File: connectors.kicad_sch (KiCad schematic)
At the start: 65 parts, among them J1 Molex_Nano-Fit_1x2_SMD_105430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, J2 Conn_FAKRA_59S2AQ-40MT5-Z_1, J3 Conn_FAKRA_59S2AQ-40MT5-Z_1, J4 Conn_FAKRA_59S2AQ-40MT5-Z_1, J5 Conn_FAKRA_59S2AQ-40MT5-Z_1, J6 Conn_FFC_WE_68715014522, Q6 DMG1012T-7, U1 SN74LV1T125DBVR, U2 SN74LV1T125DBVR, U8 NTS0102_TSSOP

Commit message: [#74135] Fix DNP malformations
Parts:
- R61, R63, R68, R69, R8: DNP DNP -> (none)
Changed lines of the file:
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@@
 			)
 		)
-		(property "DNP" "DNP"
-			(at 116.84 143.51 0)
-			(effects
-				(font
-					(size 1.27 1.27)
-				)
-				(hide yes)
-			)
-		)
 		(pin "1"
 		)
@@
 			)
 		)
-		(property "DNP" "DNP"
-			(at 116.84 139.7 0)
-			(effects
-				(font
-					(size 1.27 1.27)
-				)
-				(hide yes)
-			)
-		)
 		(pin "1"
 		)
@@
 			)
 		)
-		(property "DNP" "DNP"
-			(at 190.5 128.27 0)
-			(effects
-				(font
-					(size 1.27 1.27)
-				)
-				(hide yes)
-			)
-		)
 		(pin "1"
 		)
@@
 			)
 		)
-		(property "DNP" "DNP"
-			(at 289.56 160.02 0)
-			(effects
-				(font
-					(size 1.27 1.27)
-				)
-				(hide yes)
-			)
-		)
 		(pin "1"
 		)
@@
 				(hide yes)
 			)
-		)
-		(property "DNP" "DNP"
-			(at 184.15 128.27 0)
-			(effects
-				(font
-					(size 1.27 1.27)
-				)
-				(hide yes)
-			)

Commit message: [#74135] Clean noInBom fields
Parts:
- Q6: now in the parts list
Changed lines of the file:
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@@
 	(label "FFC_3V3"
 		(at 259.08 199.39 270)
-		(fields_autoplaced yes)
 		(effects
 			(font
@@
 	(label "VSYNC_CAM0"
 		(at 106.68 72.39 0)
-		(fields_autoplaced yes)
 		(effects
 			(font
@@
 	(label "CSI0.CLK_P"
 		(at 331.47 104.14 0)
-		(fields_autoplaced yes)
 		(effects
 			(font
@@
 	(label "MFP1"
 		(at 156.21 76.2 180)
-		(fields_autoplaced yes)
 		(effects
 			(font
@@
 	(label "MFP1"
 		(at 53.34 190.5 180)
-		(fields_autoplaced yes)
 		(effects
 			(font
@@
 	(label "MFP0"
 		(at 156.21 72.39 180)
-		(fields_autoplaced yes)
 		(effects
 			(font
@@
 	(label "CSI0.D1_N"
 		(at 331.47 88.9 0)
-		(fields_autoplaced yes)
 		(effects
 			(font
@@
 	(label "CSI1.CLK_N"
 		(at 331.47 147.32 0)
-		(fields_autoplaced yes)
 		(effects
 			(font
@@
 	(label "MFP3"
 		(at 53.34 195.58 180)
-		(fields_autoplaced yes)
 		(effects
 			(font
@@
 	(label "SCL_CAM0"
 		(at 337.82 177.8 0)
-		(fields_autoplaced yes)
 		(effects
 			(font
@@
 	(label "MFP5"
 		(at 53.34 200.66 180)
-		(fields_autoplaced yes)
 		(effects
 			(font
@@
 	(label "VSYNC_CAM1"
 		(at 261.62 162.56 0)
-		(fields_autoplaced yes)
 		(effects
 			(font
@@
 	(label "CSI0.CLK_N"
 		(at 331.47 101.6 0)
-		(fields_autoplaced yes)
 		(effects
 			(font
@@
 	(label "SCL_CAM"
 		(at 201.93 134.62 180)
-		(fields_autoplaced yes)
 		(effects
 			(font
@@
 	(label "FFC_3V3"
 		(at 190.5 113.03 270)
-		(fields_autoplaced yes)
 		(effects
 			(font
@@
 	(label "MFP7"
 		(at 53.34 203.2 180)
-		(fields_autoplaced yes)
 		(effects
 			(font
@@
 	(label "VSYNC_CAM0"
 		(at 261.62 157.48 0)
-		(fields_autoplaced yes)
 		(effects
 			(font
@@
 	(label "CSI1.D0_N"
 		(at 331.47 139.7 0)
-		(fields_autoplaced yes)
 		(effects
 			(font
@@
 	(label "CSI1.D3_N"
 		(at 331.47 124.46 0)
-		(fields_autoplaced yes)
 		(effects
 			(font
@@
 	(label "CSI0.D2_P"
 		(at 331.47 86.36 0)
-		(fields_autoplaced yes)
 		(effects
 			(font
@@
 	(label "SDA_CAM1"
 		(at 337.82 180.34 0)
-		(fields_autoplaced yes)
 		(effects
 			(font
@@
 	(label "SCL_CAM"
 		(at 292.1 177.8 0)
-		(fields_autoplaced yes)
 		(effects
 			(font
@@
 	(label "CSI0.D2_N"
 		(at 331.47 83.82 0)
-		(fields_autoplaced yes)
 		(effects
 			(font
@@
 	(label "SDA_CAM0"
 		(at 337.82 175.26 0)
-		(fields_autoplaced yes)
 		(effects
 			(font
@@
 	(label "SCL_CAM1"
 		(at 337.82 182.88 0)
-		(fields_autoplaced yes)
 		(effects
 			(font
@@
 	(label "CSI0.D0_P"
 		(at 331.47 96.52 0)
-		(fields_autoplaced yes)
 		(effects
 			(font
@@
 	(label "CSI1.CLK_P"
 		(at 331.47 149.86 0)
-		(fields_autoplaced yes)
 		(effects
 			(font
@@
 	(label "CSI0.D1_P"
 		(at 331.47 91.44 0)
-		(fields_autoplaced yes)
 		(effects
 			(font
@@
 	(label "MFP8"
 		(at 53.34 205.74 180)
-		(fields_autoplaced yes)
 		(effects
 			(font
@@
 	(label "SDA_CAM"
 		(at 201.93 132.08 180)
-		(fields_autoplaced yes)
 		(effects
 			(font
@@
 	(label "MFP7"
 		(at 101.6 139.7 0)
-		(fields_autoplaced yes)
 		(effects
 			(font
@@
 	(label "FFC_3V3"
 		(at 294.64 195.58 0)
-		(fields_autoplaced yes)
 		(effects
 			(font
@@
 	(label "CSI1.D3_P"
 		(at 331.47 127 0)
-		(fields_autoplaced yes)
 		(effects
 			(font
@@
 	(label "CSI1.D1_N"
 		(at 331.47 134.62 0)
-		(fields_autoplaced yes)
 		(effects
 			(font
@@
 	(label "CSI0.D3_P"
 		(at 331.47 81.28 0)
-		(fields_autoplaced yes)
 		(effects
 			(font
@@
 	(label "SDA_CAM"
 		(at 292.1 175.26 0)
-		(fields_autoplaced yes)
 		(effects
 			(font
@@
 	(label "CSI1.D1_P"
 		(at 331.47 137.16 0)
-		(fields_autoplaced yes)
 		(effects
 			(font
@@
 	(label "DC_UNFUSED"
 		(at 29.21 69.85 0)
-		(fields_autoplaced yes)
 		(effects
 			(font
@@
 	(label "CSI1.D2_P"
 		(at 331.47 132.08 0)
-		(fields_autoplaced yes)
 		(effects
 			(font
@@
 	(label "CSI1.D2_N"
 		(at 331.47 129.54 0)
-		(fields_autoplaced yes)
 		(effects
 			(font
@@
 	(label "MFP3"
 		(at 210.82 76.2 180)
-		(fields_autoplaced yes)
 		(effects
 			(font
@@
 	(label "MFP8"
 		(at 101.6 143.51 0)
-		(fields_autoplaced yes)
 		(effects
 			(font
@@
 	(label "MFP4"
 		(at 20.32 246.38 0)
-		(fields_autoplaced yes)
 		(effects
 			(font
@@
 	(label "CSI0.D0_N"
 		(at 331.47 93.98 0)
-		(fields_autoplaced yes)
 		(effects
 			(font
@@
 	(label "MFP0"
 		(at 53.34 187.96 180)
-		(fields_autoplaced yes)
 		(effects
 			(font
@@
 	(label "FFC_3V3"
 		(at 175.26 105.41 270)
-		(fields_autoplaced yes)
 		(effects
 			(font
@@
 	(label "MFP4"
 		(at 53.34 198.12 180)
-		(fields_autoplaced yes)
 		(effects
 			(font
@@
 	(label "CSI0.D3_N"
 		(at 331.47 78.74 0)
-		(fields_autoplaced yes)
 		(effects
 			(font
@@
 	(label "MFP2"
 		(at 210.82 72.39 180)
-		(fields_autoplaced yes)
 		(effects
 			(font
@@
 	(label "VSYNC_CAM1"
 		(at 161.29 72.39 0)
-		(fields_autoplaced yes)
 		(effects
 			(font
@@
 	(label "DC_UNFUSED"
 		(at 78.74 91.44 180)
-		(fields_autoplaced yes)
 		(effects
 			(font
@@
 	(label "CSI1.D0_P"
 		(at 331.47 142.24 0)
-		(fields_autoplaced yes)
 		(effects
 			(font
@@
 	(label "MFP2"
 		(at 53.34 193.04 180)
-		(fields_autoplaced yes)
 		(effects
 			(font
@@
 		(shape bidirectional)
 		(at 147.32 233.68 180)
-		(fields_autoplaced yes)
 		(effects
 			(font
@@
 		(shape input)
 		(at 322.58 153.67 180)
-		(fields_autoplaced yes)
 		(effects
 			(font
@@
 		(shape input)
 		(at 151.13 256.54 90)
-		(fields_autoplaced yes)
 		(effects
 			(font
@@
 		(shape input)
 		(at 151.13 209.55 90)
-		(fields_autoplaced yes)
 		(effects
 			(font
@@
 		(shape input)
 		(at 322.58 107.95 180)
-		(fields_autoplaced yes)
 		(effects
 			(font
@@
 		(shape bidirectional)
 		(at 147.32 186.69 180)
-		(fields_autoplaced yes)
 		(effects
 			(font
@@
 		(shape output)
 		(at 101.6 134.62 180)
-		(fields_autoplaced yes)
 		(effects
 			(font
@@
 		(shape bidirectional)
 		(at 101.6 132.08 180)
-		(fields_autoplaced yes)
 		(effects
 			(font
@@
 		(shape output)
 		(at 303.53 200.66 180)
-		(fields_autoplaced yes)
 		(effects
 			(font
@@
 		(shape output)
 		(at 266.7 207.01 90)
-		(fields_autoplaced yes)
 		(effects
 			(font
@@
 		(shape bidirectional)
 		(at 39.37 209.55 180)
-		(fields_autoplaced yes)
 		(effects
 			(font
@@
 		(shape bidirectional)
 		(at 147.32 210.82 180)
-		(fields_autoplaced yes)
 		(effects
 			(font
@@
 		(shape input)
 		(at 151.13 185.42 90)
-		(fields_autoplaced yes)
 		(effects
 			(font
@@
 		(shape bidirectional)
 		(at 147.32 257.81 180)
-		(fields_autoplaced yes)
 		(effects
 			(font
@@
 		(shape output)
 		(at 73.66 69.85 0)
-		(fields_autoplaced yes)
 		(effects
 			(font
@@
 		(shape input)
 		(at 151.13 232.41 90)
-		(fields_autoplaced yes)
 		(effects
 			(font
@@
 		(unit 1)
 		(exclude_from_sim no)
-		(in_bom no)
+		(in_bom yes)
 		(on_board yes)
 		(dnp no)

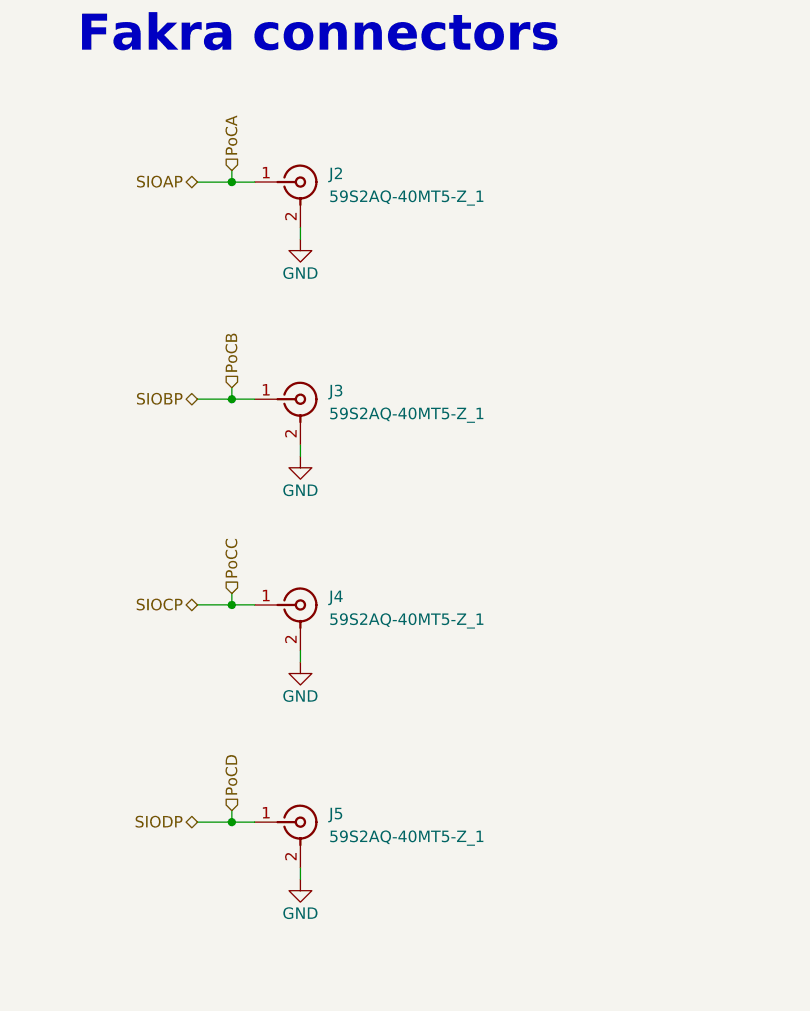
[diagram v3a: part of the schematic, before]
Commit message: [#80514] change 59S2AQ-40MT5-Z_1 connector to 7-2287906-0
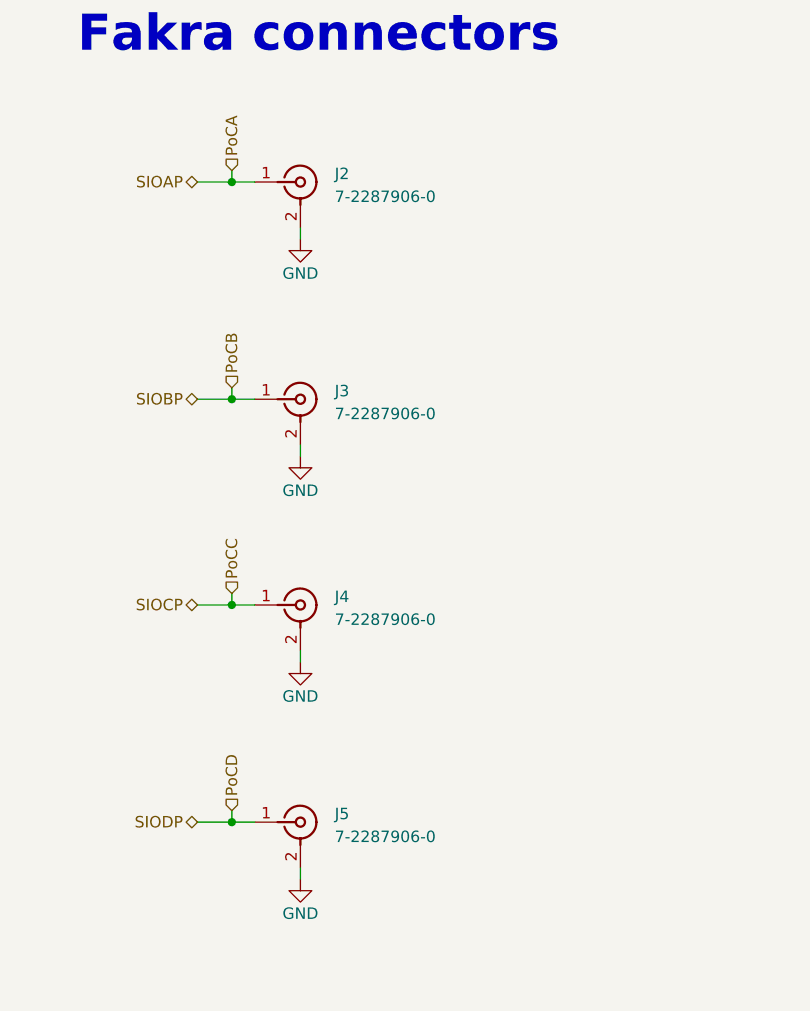
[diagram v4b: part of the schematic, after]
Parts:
- J2, J3, J4, J5: footprint antmicro-footprints:Conn_FAKRA_59S2AQ-40MT5-Z_1 -> antmicro-footprints:Conn_FAKRA_7-2287906-0; symbol antmicroCoaxialConnectorsRF:Conn_FAKRA_59S2AQ-40MT5-Z_1 -> antmicroCoaxialConnectorsRF:Conn_FAKRA_7-2287906-0; MPN 59S2AQ-40MT5-Z_1 -> 7-2287906-0; Manufacturer Rosenberger -> TE Connectivity
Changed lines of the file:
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@@
 (kicad_sch
-	(version 20231120)
+	(version 20250114)
 	(generator "eeschema")
-	(generator_version "8.0")
+	(generator_version "9.0")
 	(paper "A3")
 	(title_block
@@
 		(comment 1 "www.antmicro.com")
 	)
+	(text "Multi-function pins"
+		(exclude_from_sim no)
+		(at 21.59 177.165 0)
+		(effects
+			(font
+				(size 4 4)
+				(thickness 0.8)
+				(bold yes)
+			)
+			(justify left bottom)
+		)
+	)
+	(text "CSI connector"
+		(exclude_from_sim no)
+		(at 304.165 63.5 0)
+		(effects
+			(font
+				(size 4 4)
+				(thickness 0.8)
+				(bold yes)
+			)
+			(justify left bottom)
+		)
+	)
+	(text "Fakra connectors"
+		(exclude_from_sim no)
+		(at 133.985 172.72 0)
+		(effects
+			(font
+				(size 4 4)
+				(thickness 0.8)
+				(bold yes)
+			)
+			(justify left bottom)
+		)
+	)
+	(text "Buffer gates"
+		(exclude_from_sim no)
+		(at 143.51 40.64 0)
+		(effects
+			(font
+				(size 4 4)
+				(thickness 0.8)
+				(bold yes)
+			)
+			(justify left bottom)
+		)
+	)
+	(text "Power connector"
+		(exclude_from_sim no)
+		(at 26.035 54.61 0)
+		(effects
+			(font
+				(size 4 4)
+				(thickness 0.8)
+				(bold yes)
+			)
+			(justify left bottom)
+		)
+	)
+	(text "Level shifter"
+		(exclude_from_sim no)
+		(at 137.795 101.6 0)
+		(effects
+			(font
+				(size 4 4)
+				(thickness 0.8)
+				(bold yes)
+			)
+			(justify left bottom)
+		)
+	)
 	(junction
 		(at 289.56 157.48)
@@
 		)
 	)
-	(text "Multi-function pins"
-		(exclude_from_sim no)
-		(at 21.59 177.165 0)
-		(effects
-			(font
-				(size 4 4)
-				(thickness 0.8)
-				(bold yes)
-			)
-			(justify left bottom)
-		)
-	)
-	(text "CSI connector"
-		(exclude_from_sim no)
-		(at 304.165 63.5 0)
-		(effects
-			(font
-				(size 4 4)
-				(thickness 0.8)
-				(bold yes)
-			)
-			(justify left bottom)
-		)
-	)
-	(text "Fakra connectors"
-		(exclude_from_sim no)
-		(at 133.985 172.72 0)
-		(effects
-			(font
-				(size 4 4)
-				(thickness 0.8)
-				(bold yes)
-			)
-			(justify left bottom)
-		)
-	)
-	(text "Buffer gates"
-		(exclude_from_sim no)
-		(at 143.51 40.64 0)
-		(effects
-			(font
-				(size 4 4)
-				(thickness 0.8)
-				(bold yes)
-			)
-			(justify left bottom)
-		)
-	)
-	(text "Power connector"
-		(exclude_from_sim no)
-		(at 26.035 54.61 0)
-		(effects
-			(font
-				(size 4 4)
-				(thickness 0.8)
-				(bold yes)
-			)
-			(justify left bottom)
-		)
-	)
-	(text "Level shifter"
-		(exclude_from_sim no)
-		(at 137.795 101.6 0)
-		(effects
-			(font
-				(size 4 4)
-				(thickness 0.8)
-				(bold yes)
-			)
-			(justify left bottom)
-		)
-	)
 	(label "FFC_3V3"
 		(at 259.08 199.39 270)
@@
 	)
 	(symbol
-		(lib_id "antmicroCoaxialConnectorsRF:Conn_FAKRA_59S2AQ-40MT5-Z_1")
+		(lib_id "antmicroCoaxialConnectorsRF:Conn_FAKRA_7-2287906-0")
 		(at 153.67 210.82 0)
 		(unit 1)
@@
 		(fields_autoplaced yes)
 		(property "Reference" "J3"
-			(at 161.925 209.9066 0)
+			(at 162.56 209.9067 0)
 			(effects
 				(font
@@
 			)
 		)
-		(property "Footprint" "antmicro-footprints:Conn_FAKRA_59S2AQ-40MT5-Z_1"
+		(property "Footprint" "antmicro-footprints:Conn_FAKRA_7-2287906-0"
 			(at 173.99 220.98 0)
 			(effects
@@
 			)
 		)
-		(property "Datasheet" "https://products.rosenberger.com/radio-frequency/connectors/288881/59s2aq-40mt5-z-1-right-angle-plug-pcb-w.-housing"
+		(property "Datasheet" "https://www.te.com/en/product-7-2287906-0.html"
 			(at 173.99 223.52 0)
 			(effects
@@
 			)
 		)
-		(property "Description" "FAKRA GEN 2 PCB, SMD, Right angle plug, 50 Ohm, Z Key Code"
+		(property "Description" "FAKRA, 1 POS, ASSY EDGE MOUNT, 12OCLOCK"
 			(at 153.67 210.82 0)
 			(effects
@@
 			)
 		)
-		(property "MPN" "59S2AQ-40MT5-Z_1"
-			(at 161.925 212.4466 0)
+		(property "MPN" "7-2287906-0"
+			(at 162.56 212.4467 0)
 			(effects
 				(font
@@
 			)
 		)
-		(property "Manufacturer" "Rosenberger"
+		(property "Manufacturer" "TE Connectivity"
 			(at 173.99 228.6 0)
 			(effects
@@
 	)
 	(symbol
-		(lib_id "antmicroCoaxialConnectorsRF:Conn_FAKRA_59S2AQ-40MT5-Z_1")
+		(lib_id "antmicroCoaxialConnectorsRF:Conn_FAKRA_7-2287906-0")
 		(at 153.67 233.68 0)
 		(unit 1)
@@
 		(fields_autoplaced yes)
 		(property "Reference" "J4"
-			(at 161.925 232.7666 0)
+			(at 162.56 232.7667 0)
 			(effects
 				(font
@@
 			)
 		)
-		(property "Footprint" "antmicro-footprints:Conn_FAKRA_59S2AQ-40MT5-Z_1"
+		(property "Footprint" "antmicro-footprints:Conn_FAKRA_7-2287906-0"
 			(at 173.99 243.84 0)
 			(effects
@@
 			)
 		)
-		(property "Datasheet" "https://products.rosenberger.com/radio-frequency/connectors/288881/59s2aq-40mt5-z-1-right-angle-plug-pcb-w.-housing"
+		(property "Datasheet" "https://www.te.com/en/product-7-2287906-0.html"
 			(at 173.99 246.38 0)
 			(effects
@@
 			)
 		)
-		(property "Description" "FAKRA GEN 2 PCB, SMD, Right angle plug, 50 Ohm, Z Key Code"
+		(property "Description" "FAKRA, 1 POS, ASSY EDGE MOUNT, 12OCLOCK"
 			(at 153.67 233.68 0)
 			(effects
@@
 			)
 		)
-		(property "MPN" "59S2AQ-40MT5-Z_1"
-			(at 161.925 235.3066 0)
+		(property "MPN" "7-2287906-0"
+			(at 162.56 235.3067 0)
 			(effects
 				(font
@@
 			)
 		)
-		(property "Manufacturer" "Rosenberger"
+		(property "Manufacturer" "TE Connectivity"
 			(at 173.99 251.46 0)
 			(effects
@@
 	)
 	(symbol
-		(lib_id "antmicroCoaxialConnectorsRF:Conn_FAKRA_59S2AQ-40MT5-Z_1")
+		(lib_id "antmicroCoaxialConnectorsRF:Conn_FAKRA_7-2287906-0")
 		(at 153.67 186.69 0)
 		(unit 1)
@@
 		(fields_autoplaced yes)
 		(property "Reference" "J2"
-			(at 161.925 185.7766 0)
+			(at 162.56 185.7767 0)
 			(effects
 				(font
@@
 			)
 		)
-		(property "Footprint" "antmicro-footprints:Conn_FAKRA_59S2AQ-40MT5-Z_1"
+		(property "Footprint" "antmicro-footprints:Conn_FAKRA_7-2287906-0"
 			(at 173.99 196.85 0)
 			(effects
@@
 			)
 		)
-		(property "Datasheet" "https://products.rosenberger.com/radio-frequency/connectors/288881/59s2aq-40mt5-z-1-right-angle-plug-pcb-w.-housing"
+		(property "Datasheet" "https://www.te.com/en/product-7-2287906-0.html"
 			(at 173.99 199.39 0)
 			(effects
@@
 			)
 		)
-		(property "Description" "FAKRA GEN 2 PCB, SMD, Right angle plug, 50 Ohm, Z Key Code"
+		(property "Description" "FAKRA, 1 POS, ASSY EDGE MOUNT, 12OCLOCK"
 			(at 153.67 186.69 0)
 			(effects
@@
 			)
 		)
-		(property "MPN" "59S2AQ-40MT5-Z_1"
-			(at 161.925 188.3166 0)
+		(property "MPN" "7-2287906-0"
+			(at 162.56 188.3167 0)
 			(effects
 				(font
@@
 			)
 		)
-		(property "Manufacturer" "Rosenberger"
+		(property "Manufacturer" "TE Connectivity"
 			(at 173.99 204.47 0)
 			(effects
@@
 	)
 	(symbol
-		(lib_id "antmicroCoaxialConnectorsRF:Conn_FAKRA_59S2AQ-40MT5-Z_1")
+		(lib_id "antmicroCoaxialConnectorsRF:Conn_FAKRA_7-2287906-0")
 		(at 153.67 257.81 0)
 		(unit 1)
@@
 		(fields_autoplaced yes)
 		(property "Reference" "J5"
-			(at 161.925 256.8966 0)
+			(at 162.56 256.8967 0)
 			(effects
 				(font
@@
 			)
 		)
-		(property "Footprint" "antmicro-footprints:Conn_FAKRA_59S2AQ-40MT5-Z_1"
+		(property "Footprint" "antmicro-footprints:Conn_FAKRA_7-2287906-0"
 			(at 173.99 267.97 0)
 			(effects
@@
 			)
 		)
-		(property "Datasheet" "https://products.rosenberger.com/radio-frequency/connectors/288881/59s2aq-40mt5-z-1-right-angle-plug-pcb-w.-housing"
+		(property "Datasheet" "https://www.te.com/en/product-7-2287906-0.html"
 			(at 173.99 270.51 0)
 			(effects
@@
 			)
 		)
-		(property "Description" "FAKRA GEN 2 PCB, SMD, Right angle plug, 50 Ohm, Z Key Code"
+		(property "Description" "FAKRA, 1 POS, ASSY EDGE MOUNT, 12OCLOCK"
 			(at 153.67 257.81 0)
 			(effects
@@
 			)
 		)
-		(property "MPN" "59S2AQ-40MT5-Z_1"
-			(at 161.925 259.4366 0)
+		(property "MPN" "7-2287906-0"
+			(at 162.56 259.4367 0)
 			(effects
 				(font
@@
 			)
 		)
-		(property "Manufacturer" "Rosenberger"
+		(property "Manufacturer" "TE Connectivity"
 			(at 173.99 275.59 0)
 			(effects
